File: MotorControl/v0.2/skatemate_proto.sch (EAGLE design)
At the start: 104 parts, among them IC1 REG1117, Q1 IRF740, Q2 IRF740, Q3 IRF740, Q4 IRF740, Q5 IRF740, Q6 IRF740, U1 DRV8301DCAR

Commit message: layouting on v0.2
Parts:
- removed Q1, Q2, Q3, Q4, Q5, Q6: IRF740, transistor-power:IRF740
- removed SV1, SV2: (no value), skatemate:MA12-1
- added C39: 2u2, skatemate:C-EUC1206
- TP1: value TPSMD_M_1006 -> SUPPLY
- TP2: value TPSMD_M_1006 -> GND
- TP3: value TPSMD_M_1006 -> PH_A
- TP4: value TPSMD_M_1006 -> PH_B
- TP5: value TPSMD_M_1006 -> PH_C
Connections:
- net +5V: no longer SV1.3
- net ASENSE: no longer SV2.9
- net BSENSE: no longer SV2.10
- net CSENSE: no longer SV2.11
- net DRV_DCCAL: no longer SV1.11
- net DRV_EN_GATE: no longer SV1.12
- net DRV_NCS: no longer SV1.7
- net DRV_NFAULT: no longer SV1.6
- net DRV_NOCTW: no longer SV1.5
- net DRV_PWRGD: no longer SV1.4
- net DRV_SCK: no longer SV1.10
- net DRV_SDI: no longer SV1.8
- net DRV_SDO: no longer SV1.9
- net DRV_SOA: no longer SV2.7
- net DRV_SOB: no longer SV2.8
- net GND: now also C39.2; no longer Q6.S, SV1.2
- net INH_A: no longer SV2.1
- net INH_B: no longer SV2.3
- net INH_C: no longer SV2.5
- net INL_A: no longer SV2.2
- net INL_B: no longer SV2.4
- net INL_C: no longer SV2.6
- net N$10: no longer Q2.G
- net N$11: no longer Q3.G
- net N$12: no longer Q6.G
- net N$7: no longer Q1.G
- net N$8: no longer Q4.G
- net N$9: no longer Q5.G
- net PH_A: no longer Q1.S, Q4.D
- net PH_B: no longer Q2.S, Q5.D
- net PH_C: no longer Q3.S, Q6.D
- net SN_A: no longer Q4.S
- net SN_B: no longer Q5.S
- net SSENSE: no longer SV2.12
- net SUPPLY: now also C39.1; no longer Q1.D, Q2.D, Q3.D
- net VCC: no longer SV1.1
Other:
- moved on the sheet: C6, C7, C8, TP4, TP5, U$4, U$5, U$6, U$7, U$8, U$9

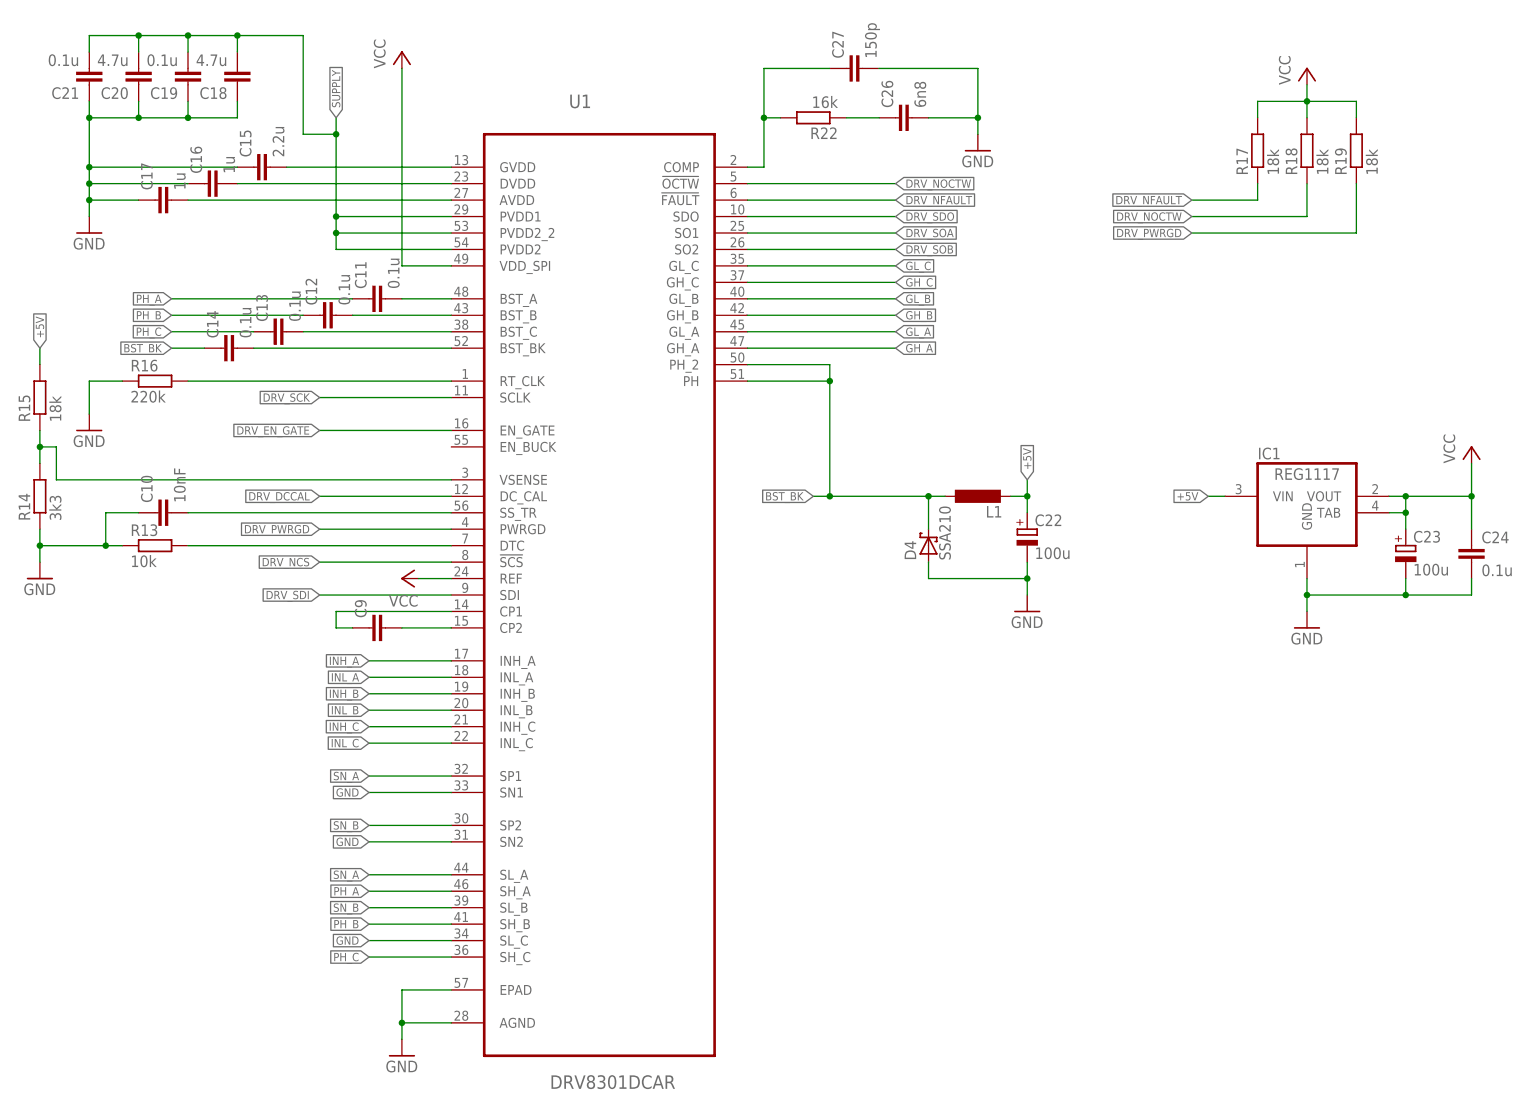
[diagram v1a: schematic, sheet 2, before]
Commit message: Parts renumber and BOM ULP
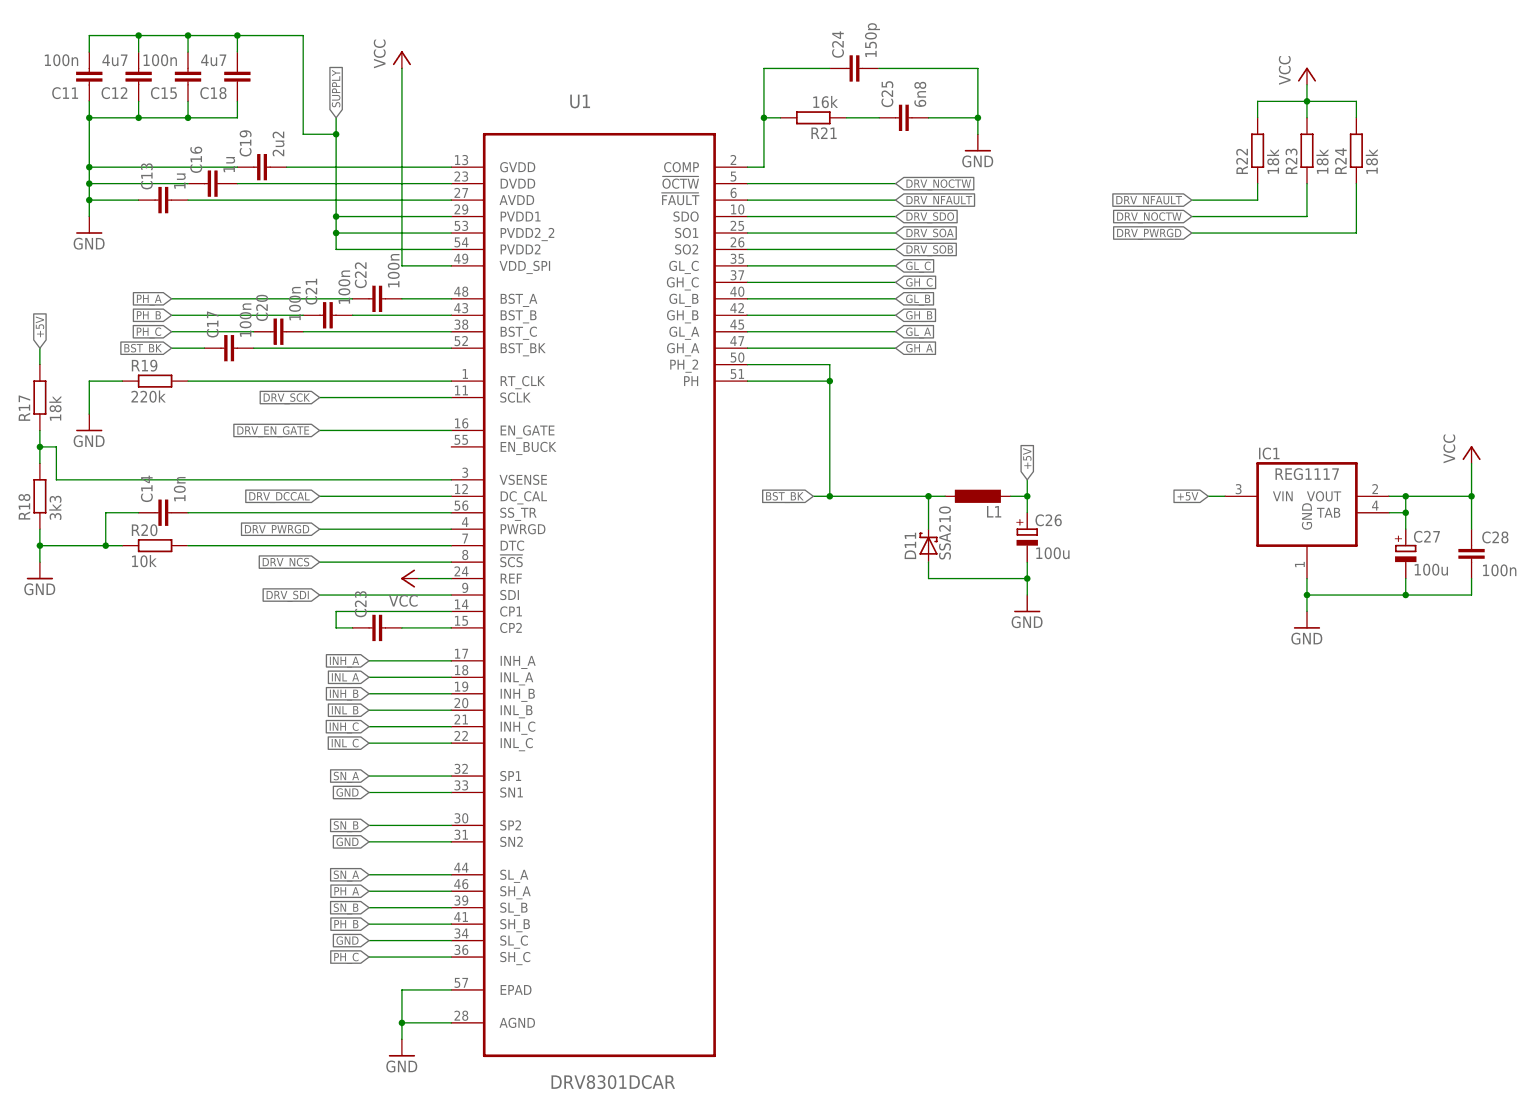
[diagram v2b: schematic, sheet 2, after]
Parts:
- removed R33: 3k3, skatemate:R-EU_R0805
- removed U$1, U$2: R_EU, skatemate:R_EU
- removed U$4, U$5, U$6, U$7, U$8: IRFS7534, skatemate:IRFS7534
- added D10, D7, D8, D9: BAS85, skatemate:SCHOTTKY-DIODESOD80C
- added D11: SSA210, skatemate:SCHOTTKY-DIODEDO-214AA
- added R28: 0 *, skatemate:R-EU_R0805
- added R29: 1k5, skatemate:R-EU_R0805
- added R30: 22, skatemate:R-EU_R0805
- C10: value 10nF -> 47p
- C11, C21: value 0.1u -> 100n
- C12: value 0.1u -> 4u7; device skatemate:C-EUC0805 -> skatemate:C-EUC1206
- C13: value 0.1u -> 1u; device skatemate:C-EUC0805 -> skatemate:C-EUC1206
- C14: value 0.1u -> 10n
- C15: value 2.2u -> 100n; device skatemate:C-EUC1206 -> skatemate:C-EUC0805
- C17: value 1u -> 100n; device skatemate:C-EUC1206 -> skatemate:C-EUC0805
- C18: value 4.7u -> 4u7
- C19: value 0.1u -> 2u2; device skatemate:C-EUC0805 -> skatemate:C-EUC1206
- C2: value (none) -> 2u2; device skatemate:C-EUC0805 -> skatemate:C-EUC1206
- C20: value 4.7u -> 100n; device skatemate:C-EUC1206 -> skatemate:C-EUC0805
- C22: value 100u -> 100n; device skatemate:CPOL-EUB/3528-21W -> skatemate:C-EUC0805
- C23: value 100u -> (none); device skatemate:CPOL-EUB/3528-21W -> skatemate:C-EUC0805
- C24: value 0.1u -> 150p
- C25: value 47p -> 6n8
- C26: value 6n8 -> 100u; device skatemate:C-EUC0805 -> skatemate:CPOL-EUB/3528-21W
- C27: value 150p -> 100u; device skatemate:C-EUC0805 -> skatemate:CPOL-EUB/3528-21W
- C28, C33, C34: value 2u2 -> 100n
- C29: value 2u2 -> 22p
- C3, C4, C5: value 47p -> 2u2; device skatemate:C-EUC0805 -> skatemate:C-EUC1206
- C30: value 100n -> 22p
- C31, C32, C36: value 100n -> 2u2
- C37: value 22p -> 2u2
- C38: value 22p -> 100n
- C39: value 2u2 -> 100n; device skatemate:C-EUC1206 -> skatemate:C-EUC0805
- C6: value 2u2 -> (none); device skatemate:C-EUC1206 -> skatemate:C-EUC0805
- C7, C8: value 2u2 -> 47p; device skatemate:C-EUC1206 -> skatemate:C-EUC0805
- C9: value (none) -> 47p
- D1, D2, D3, D5: value BAS85 -> IRFS7534; device skatemate:SCHOTTKY-DIODESOD80C -> skatemate:IRFS7534
- D4: value SSA210 -> IRFS7534; device skatemate:SCHOTTKY-DIODEDO-214AA -> skatemate:IRFS7534
- R13: value 10k -> 39k
- R14: value 3k3 -> 2k2
- R15: value 18k -> 39k
- R16: value 220k -> 2k2
- R18: value 18k -> 3k3
- R19: value 18k -> 220k
- R20: value 39k -> 10k
- R21: value 2k2 -> 16k
- R22: value 16k -> 18k
- R23: value 100k -> 18k
- R24: value 22 -> 18k
- R25: value 22 -> 3k3
- R26: value 1k5 -> 3k3
- R27: value 0 * -> 3k3
- R3, R6: value (none) -> R_EU; device skatemate:R-EU_R0805 -> skatemate:R_EU
- R31: value 3k3 -> 22
- R32: value 3k3 -> 100k
- R7: value 39k -> (none)
- R8: value 2k2 -> (none)
- renumbered LED4 to LED1, LED5 to LED2, LED6 to LED3, SV3 to SV1, U$10 to X1, U$3 to U2, U$9 to D6
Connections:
- net +5V: now also C26.+, R17.2; no longer C22.+, R15.2
- net ASENSE: now also C7.1, D7.A, R10.2, R9.1; no longer C3.1, D1.A, R7.1, R8.2
- net BSENSE: now also C8.1, D8.A, R11.1, R12.2; no longer C4.1, D2.A, R10.2, R9.1
- net BST_BK: now also C17.1, D11.C; no longer C14.1, D4.C
- net CSENSE: now also C9.1, D9.A, R13.1, R14.2; no longer C5.1, D3.A, R11.1, R12.2
- net DRV_NFAULT: now also R22.1; no longer R17.1
- net DRV_NOCTW: now also R23.1; no longer R18.1
- net DRV_PWRGD: now also R24.1; no longer R19.1
- net GH_B: now also R4.1; no longer R3.1
- net GH_C: now also R7.1; no longer R5.1
- net GL_B: now also R5.1; no longer R4.1
- net GL_C: now also R8.1; no longer R6.1
- net GND: now also C10.2, C11.1, C12.1, C13.1, C14.1, C26.-, C27.-, C28.2, C39.1, C9.2, D11.A, R18.1, R19.1, R20.1, R3.2, R32.2, R6.2; no longer C10.1, C17.1, C20.1, C21.1, C22.-, C23.-, C26.2, C27.2, C28.1, C39.2, D4.A, R13.1, R21.1, R23.2, R8.1, U$1.2, U$2.2
- net N$1: now also C23.2; no longer C9.2
- net N$10: now also D3.G, R4.2; no longer R3.2, U$6.G
- net N$11: now also D5.G, R7.2; no longer R5.2, U$8.G
- net N$12: now also R8.2; no longer R6.2
- net N$13: now also C22.2; no longer C11.2
- net N$14: now also C21.2; no longer C12.2
- net N$15: now also C20.2; no longer C13.2
- net N$16: now also C17.2; no longer C14.2
- net N$17: now also C19.2; no longer C15.2
- net N$19: now also C13.2; no longer C17.2
- net N$2: now also C23.1; no longer C9.1
- net N$20: now also C24.1, R21.2; no longer C27.1, R22.2
- net N$21: now also C25.1, R21.1; no longer C26.1, R22.1
- net N$22: now also R32.1; no longer R23.1
- net N$23: now also R29.1, R31.1; no longer R24.1, R26.1
- net N$24: now also R30.1; no longer R25.1
- net N$25: now also R28.1; no longer R27.1
- net N$28: now also R27.2; no longer R33.2
- net N$29: now also R26.2; no longer R32.2
- net N$3: now also R20.2; no longer R13.2
- net N$30: now also R25.2; no longer R31.2
- net N$31: now also R25.1; no longer R31.1
- net N$32: now also R26.1; no longer R32.1
- net N$33: now also R27.1; no longer R33.1
- net N$35: now also C30.2; no longer C38.2
- net N$36: now also C29.2; no longer C37.2
- net N$4: now also R17.1, R18.2; no longer R14.2, R15.1
- net N$5: now also C14.2; no longer C10.2
- net N$6: now also R19.2; no longer R16.2
- net N$7: now also D1.G; no longer U$4.G
- net N$8: now also D2.G; no longer U$5.G
- net N$9: now also D4.G, R5.2; no longer R4.2, U$7.G
- net PH_A: now also C22.1, D1.S, D2.D, R9.2; no longer C11.1, R7.2, U$4.S, U$5.D
- net PH_B: now also C21.1, D3.S, D4.D, R11.2; no longer C12.1, R9.2, U$6.S, U$7.D
- net PH_C: now also C20.1, D5.S, R13.2; no longer C13.1, R11.2, U$8.S
- net SN_A: now also D2.S, R3.1; no longer U$1.1, U$5.S
- net SN_B: now also C6.1, D4.S, R6.1; no longer C2.1, U$2.1, U$7.S
- net SSENSE: now also C10.1, D10.A, R15.1, R16.2; no longer C25.1, D5.A, R20.1, R21.2
- net SUPPLY: now also C11.2, C12.2, C15.2, C2.1, C3.1, C4.1, C5.1, D1.D, D3.D, D5.D, R15.2; no longer C19.2, C20.2, C21.2, C39.1, C6.1, C7.1, C8.1, R20.2, U$4.D, U$6.D, U$8.D
- net USB_D+: now also R31.2; no longer R24.2
- net USB_D-: now also R30.2; no longer R25.2
- net VCC: now also C27.+, C28.1, C37.2, C38.2, C39.2, D10.C, D7.C, D8.C, D9.C, R22.2, R23.2, R24.2, R28.2, R29.2; no longer C23.+, C24.1, C28.2, C29.2, C30.2, D1.C, D2.C, D3.C, D5.C, R17.2, R18.2, R19.2, R26.2, R27.2
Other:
- moved on the sheet: C11, C12, C13, C14, C15, C17, C19, C2, C20, C21, C24, C29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
